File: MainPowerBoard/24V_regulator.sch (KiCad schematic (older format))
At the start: 14 parts, among them U1 LMR16030S

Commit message: Updated 5V regulator. Added 0Ohm resistors for all signals. Added protection zeners and diodes on battery inputs and on regulator outputs. TODO: Finish component selection.
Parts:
- removed R1: 45.3k, Resistors_SMD:R_1206_HandSoldering, symbol R
- added D203: 18V, symbol ZENER
- added D204: 30V, symbol ZENER
- added D205: DIODE, symbol DIODE
- added R201: 0, symbol R
- added R202: 47.5k, Resistors_SMD:R_1206_HandSoldering, symbol R
- L201: renamed from L1; value INDUCTOR -> 39uH
- renumbered C1 to C201, C2 to C202, C3 to C203, C4 to C204, C5 to C205, C6 to C206, D1 to D201, D2 to D202, R2 to R203, R2 to R204, U1 to U201, VR1 to VR201
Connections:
- wire segments 36 -> 44
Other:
- note removed: "Make these 1206 SMT"
- moved on the sheet: R1404

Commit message: Updated MainPowerBoard with various component footings. Added protective circuitry. Revised minor design elements.
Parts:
- removed D202: LED, hyperCustom:D_1206_HandSoldering, symbol LED-RESCUE-MainPowerBoard
- added D?: GREEN, LEDs:LED_1206, symbol LED

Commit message: Added all standard footprints to components. Finalized protection circuitry and indicator circuits.
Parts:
- removed D205: DIODE, symbol DIODE
- D203: footprint (none) -> Diodes_SMD:SMB_Handsoldering; DigiKey PN (none) -> 1SMB5931B-13DICT-ND; Mfg. (none) -> Diodes; Mfg. PN (none) -> 1SMB5931B-13
- D204: footprint (none) -> Diodes_SMD:SMB_Handsoldering; DigiKey PN (none) -> 3SMBJ5936BTPMSCT-ND; Mfg. (none) -> Micro; Mfg. PN (none) -> 3SMBJ5936B-TP
- R201: DigiKey PN (none) -> 311-0.0ERCT-ND; Mfg. (none) -> Yageo; Mfg. PN (none) -> RC1206JR-070RL
- U201: DigiKey PN (none) -> 296-44514-5-ND; Mfg. (none) -> Texas Instruments; Mfg. PN (none) -> LMR16030SDDA
- gave numbers to parts that had none: 1
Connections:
- wire segments 44 -> 42

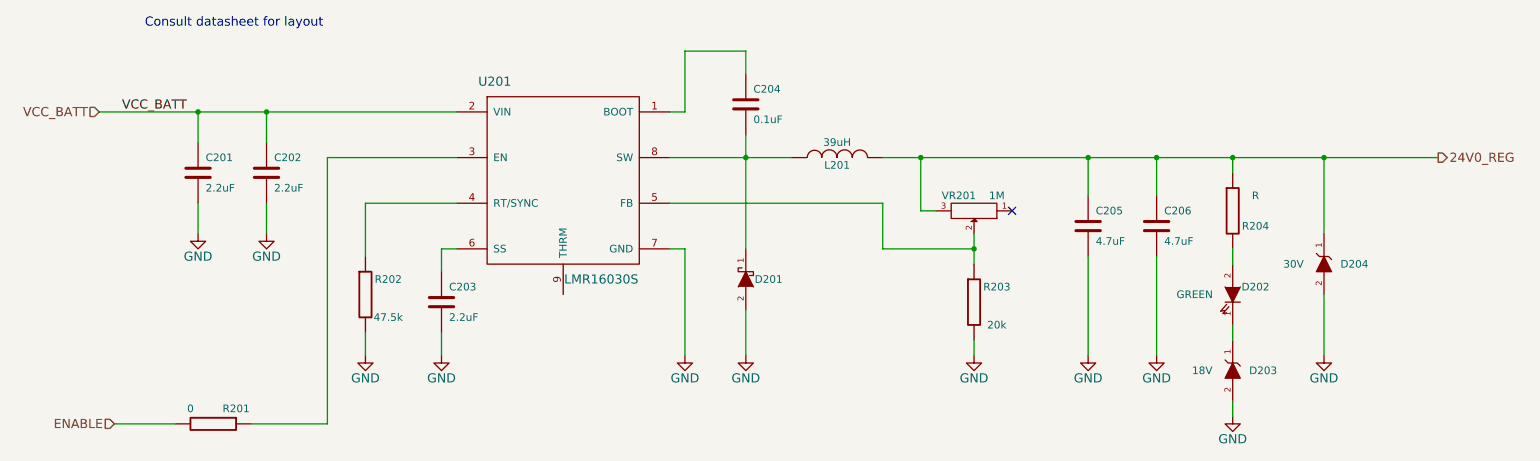
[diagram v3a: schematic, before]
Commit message: Minor changes to MainPowerBoard. About to start layout.
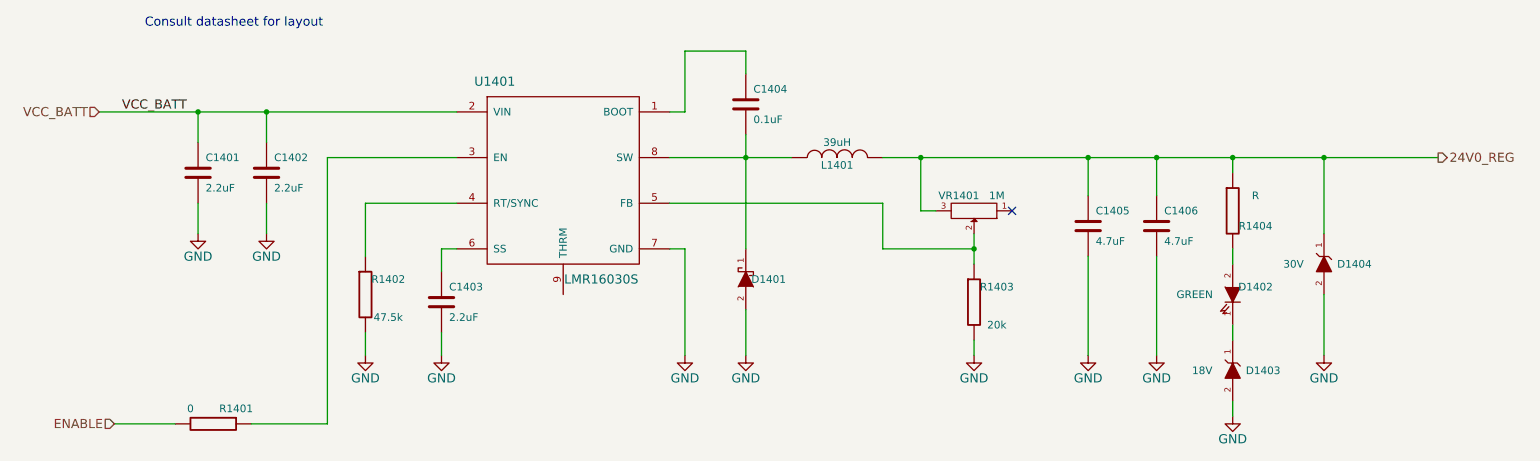
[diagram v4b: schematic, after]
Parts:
- U201: footprint (none) -> LMR16030S_8-PowerSOIC_TI.kicad_mod
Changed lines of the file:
@@
 AR Path="/583A9416/5833A728" Ref="R1304"  Part="1"
 AR Path="/583A941B/5833A728" Ref="R1404"  Part="1"
-F 0 "R204" H 8750 3950 50  0000 C CNN
+F 0 "R1404" H 8750 3950 50  0000 C CNN
 F 1 "R" H 8750 4150 50  0000 C CNN
 F 2 "Resistors_SMD:R_1210" V 8530 4050 30  0001 C CNN
@@
 AR Path="/583A9416/583A8678" Ref="U1301"  Part="1"
 AR Path="/583A941B/583A8678" Ref="U1401"  Part="1"
-F 0 "U201" H 3750 4500 60  0000 C CNN
+F 0 "U1401" H 3750 4500 60  0000 C CNN
 F 1 "LMR16030S" H 4450 3200 60  0000 C CNN
-F 2 "" H 4150 3850 60  0000 C CNN
+F 2 "LMR16030S_8-PowerSOIC_TI.kicad_mod" H 4150 3850 60  0001 C CNN
 F 3 "" H 4150 3850 60  0000 C CNN
 F 4 "Texas Instruments" H 4150 3850 60  0001 C CNN "Mfg."
@@
 AR Path="/583A9416/583A8A9A" Ref="C1301"  Part="1"
 AR Path="/583A941B/583A8A9A" Ref="C1401"  Part="1"
-F 0 "C201" H 1850 3900 50  0000 L CNN
+F 0 "C1401" H 1850 3900 50  0000 L CNN
 F 1 "2.2uF" H 1850 3700 50  0000 L CNN
 F 2 "Capacitors_SMD:C_1210_HandSoldering" H 1838 3650 30  0001 C CNN
@@
 AR Path="/583A9416/583A8B4B" Ref="C1302"  Part="1"
 AR Path="/583A941B/583A8B4B" Ref="C1402"  Part="1"
-F 0 "C202" H 2300 3900 50  0000 L CNN
+F 0 "C1402" H 2300 3900 50  0000 L CNN
 F 1 "2.2uF" H 2300 3700 50  0000 L CNN
 F 2 "Capacitors_SMD:C_1210_HandSoldering" H 2288 3650 30  0001 C CNN
@@
 AR Path="/583A9416/583A8BF8" Ref="#PWR1301"  Part="1"
 AR Path="/583A941B/583A8BF8" Ref="#PWR1401"  Part="1"
-F 0 "#PWR201" H 1800 3950 60  0001 C CNN
+F 0 "#PWR1401" H 1800 3950 60  0001 C CNN
 F 1 "GND" H 1800 4050 60  0000 C CNN
 F 2 "" H 1800 4200 60  0000 C CNN
@@
 AR Path="/583A9416/583A8C28" Ref="#PWR1302"  Part="1"
 AR Path="/583A941B/583A8C28" Ref="#PWR1402"  Part="1"
-F 0 "#PWR202" H 2250 3950 60  0001 C CNN
+F 0 "#PWR1402" H 2250 3950 60  0001 C CNN
 F 1 "GND" H 2250 4050 60  0000 C CNN
 F 2 "" H 2250 4200 60  0000 C CNN
@@
 AR Path="/583A9416/583A8CF1" Ref="C1303"  Part="1"
 AR Path="/583A941B/583A8CF1" Ref="C1403"  Part="1"
-F 0 "C203" H 3450 4750 50  0000 L CNN
+F 0 "C1403" H 3450 4750 50  0000 L CNN
 F 1 "2.2uF" H 3450 4550 50  0000 L CNN
 F 2 "Resistors_SMD:R_0805_HandSoldering" H 3438 4500 30  0001 C CNN
@@
 AR Path="/583A9416/583A8E72" Ref="#PWR1303"  Part="1"
 AR Path="/583A941B/583A8E72" Ref="#PWR1403"  Part="1"
-F 0 "#PWR203" H 2900 4750 60  0001 C CNN
+F 0 "#PWR1403" H 2900 4750 60  0001 C CNN
 F 1 "GND" H 2900 4850 60  0000 C CNN
 F 2 "" H 2900 5000 60  0000 C CNN
@@
 AR Path="/583A9416/583A8EBE" Ref="#PWR1304"  Part="1"
 AR Path="/583A941B/583A8EBE" Ref="#PWR1404"  Part="1"
-F 0 "#PWR204" H 3400 4750 60  0001 C CNN
+F 0 "#PWR1404" H 3400 4750 60  0001 C CNN
 F 1 "GND" H 3400 4850 60  0000 C CNN
 F 2 "" H 3400 5000 60  0000 C CNN
@@
 AR Path="/583A9416/583B27BB" Ref="#PWR1305"  Part="1"
 AR Path="/583A941B/583B27BB" Ref="#PWR1405"  Part="1"
-F 0 "#PWR205" H 5000 4750 60  0001 C CNN
+F 0 "#PWR1405" H 5000 4750 60  0001 C CNN
 F 1 "GND" H 5000 4850 60  0000 C CNN
 F 2 "" H 5000 5000 60  0000 C CNN
@@
 AR Path="/583A9416/583B2967" Ref="R1303"  Part="1"
 AR Path="/583A941B/583B2967" Ref="R1403"  Part="1"
-F 0 "R203" H 7050 4750 50  0000 C CNN
+F 0 "R1403" H 7050 4750 50  0000 C CNN
 F 1 "20k" H 7050 4500 50  0000 C CNN
 F 2 "Resistors_SMD:R_1206_HandSoldering" V 6830 4650 30  0001 C CNN
@@
 AR Path="/583A9416/583B2A2E" Ref="VR1301"  Part="1"
 AR Path="/583A941B/583B2A2E" Ref="VR1401"  Part="1"
-F 0 "VR201" H 7000 3950 50  0000 C CNN
+F 0 "VR1401" H 7000 3950 50  0000 C CNN
 F 1 "1M" H 6750 3950 50  0000 C CNN
 F 2 "" H 6900 4050 60  0000 C CNN
@@
 AR Path="/583A9416/583B2BCB" Ref="D1301"  Part="1"
 AR Path="/583A941B/583B2BCB" Ref="D1401"  Part="1"
-F 0 "D201" V 5400 4350 50  0000 C CNN
+F 0 "D1401" V 5400 4350 50  0000 C CNN
 F 1 "DIODESCH" H 5400 4400 50  0001 C CNN
 F 2 "Diodes_SMD:SMA_Handsoldering" H 5400 4500 60  0001 C CNN
@@
 AR Path="/583A9416/583B2C66" Ref="#PWR1306"  Part="1"
 AR Path="/583A941B/583B2C66" Ref="#PWR1406"  Part="1"
-F 0 "#PWR206" H 5400 4750 60  0001 C CNN
+F 0 "#PWR1406" H 5400 4750 60  0001 C CNN
 F 1 "GND" H 5400 4850 60  0000 C CNN
 F 2 "" H 5400 5000 60  0000 C CNN
@@
 AR Path="/583A9416/583B2D59" Ref="L1301"  Part="1"
 AR Path="/583A941B/583B2D59" Ref="L1401"  Part="1"
-F 0 "L201" V 5950 3700 50  0000 C CNN
+F 0 "L1401" V 5950 3700 50  0000 C CNN
 F 1 "39uH" V 6100 3700 50  0000 C CNN
 F 2 "" H 6000 3700 60  0000 C CNN
@@
 AR Path="/583A9416/583B307C" Ref="#PWR1307"  Part="1"
 AR Path="/583A941B/583B307C" Ref="#PWR1407"  Part="1"
-F 0 "#PWR207" H 6900 4750 60  0001 C CNN
+F 0 "#PWR1407" H 6900 4750 60  0001 C CNN
 F 1 "GND" H 6900 4850 60  0000 C CNN
 F 2 "" H 6900 5000 60  0000 C CNN
@@
 AR Path="/583A9416/583B399E" Ref="C1304"  Part="1"
 AR Path="/583A941B/583B399E" Ref="C1404"  Part="1"
-F 0 "C204" H 5450 3450 50  0000 L CNN
+F 0 "C1404" H 5450 3450 50  0000 L CNN
 F 1 "0.1uF" H 5450 3250 50  0000 L CNN
 F 2 "Resistors_SMD:R_1206_HandSoldering" H 5438 3200 30  0001 C CNN
@@
 AR Path="/583A9416/583B4188" Ref="C1305"  Part="1"
 AR Path="/583A941B/583B4188" Ref="C1405"  Part="1"
-F 0 "C205" H 7700 4250 50  0000 L CNN
+F 0 "C1405" H 7700 4250 50  0000 L CNN
 F 1 "4.7uF" H 7700 4050 50  0000 L CNN
 F 2 "Capacitors_SMD:C_1206_HandSoldering" H 7688 4000 30  0001 C CNN
@@
 AR Path="/583A9416/583B42A9" Ref="#PWR1308"  Part="1"
 AR Path="/583A941B/583B42A9" Ref="#PWR1408"  Part="1"
-F 0 "#PWR208" H 7650 4750 60  0001 C CNN
+F 0 "#PWR1408" H 7650 4750 60  0001 C CNN
 F 1 "GND" H 7650 4850 60  0000 C CNN
 F 2 "" H 7650 5000 60  0000 C CNN
@@
 AR Path="/583A9416/583B43AD" Ref="C1306"  Part="1"
 AR Path="/583A941B/583B43AD" Ref="C1406"  Part="1"
-F 0 "C206" H 8150 4250 50  0000 L CNN
+F 0 "C1406" H 8150 4250 50  0000 L CNN
 F 1 "4.7uF" H 8150 4050 50  0000 L CNN
 F 2 "Capacitors_SMD:C_1206_HandSoldering" H 8138 4000 30  0001 C CNN
@@
 AR Path="/583A9416/583B449E" Ref="#PWR1309"  Part="1"
 AR Path="/583A941B/583B449E" Ref="#PWR1409"  Part="1"
-F 0 "#PWR209" H 8100 4750 60  0001 C CNN
+F 0 "#PWR1409" H 8100 4750 60  0001 C CNN
 F 1 "GND" H 8100 4850 60  0000 C CNN
 F 2 "" H 8100 5000 60  0000 C CNN
@@
 AR Path="/583A9416/583D36BC" Ref="R1301"  Part="1"
 AR Path="/583A941B/583D36BC" Ref="R1401"  Part="1"
-F 0 "R201" V 1800 5600 50  0000 C CNN
+F 0 "R1401" V 1800 5600 50  0000 C CNN
 F 1 "0" V 1800 5300 50  0000 C CNN
 F 2 "" V 1830 5450 30  0000 C CNN
@@
 AR Path="/583A9416/583D8D48" Ref="D1303"  Part="1"
 AR Path="/583A941B/583D8D48" Ref="D1403"  Part="1"
-F 0 "D203" V 8600 4900 50  0000 C CNN
+F 0 "D1403" V 8600 4900 50  0000 C CNN
 F 1 "18V" V 8600 5300 50  0000 C CNN
 F 2 "Diodes_SMD:SMB_Handsoldering" H 8600 5100 60  0001 C CNN
@@
 AR Path="/583A9416/583D8F40" Ref="#PWR1310"  Part="1"
 AR Path="/583A941B/583D8F40" Ref="#PWR1410"  Part="1"
-F 0 "#PWR210" H 8600 5150 60  0001 C CNN
+F 0 "#PWR1410" H 8600 5150 60  0001 C CNN
 F 1 "GND" H 8600 5250 60  0000 C CNN
 F 2 "" H 8600 5400 60  0000 C CNN
@@
 AR Path="/583A9416/583D986C" Ref="D1304"  Part="1"
 AR Path="/583A941B/583D986C" Ref="D1404"  Part="1"
-F 0 "D204" V 9200 4200 50  0000 C CNN
+F 0 "D1404" V 9200 4200 50  0000 C CNN
 F 1 "30V" V 9200 4600 50  0000 C CNN
 F 2 "Diodes_SMD:SMB_Handsoldering" H 9200 4400 60  0001 C CNN
@@
 AR Path="/583A9416/583D98F6" Ref="#PWR1311"  Part="1"
 AR Path="/583A941B/583D98F6" Ref="#PWR1411"  Part="1"
-F 0 "#PWR211" H 9200 4750 60  0001 C CNN
+F 0 "#PWR1411" H 9200 4750 60  0001 C CNN
 F 1 "GND" H 9200 4850 60  0000 C CNN
 F 2 "" H 9200 5000 60  0000 C CNN
@@
 AR Path="/583A9416/583E258D" Ref="R1302"  Part="1"
 AR Path="/583A941B/583E258D" Ref="R1402"  Part="1"
-F 0 "R202" H 3050 4700 50  0000 C CNN
+F 0 "R1402" H 3050 4700 50  0000 C CNN
 F 1 "47.5k" H 3050 4450 50  0000 C CNN
 F 2 "Resistors_SMD:R_1206_HandSoldering" V 2830 4600 30  0001 C CNN
@@
 P 8600 4600
 AR Path="/582171B3/583D0112" Ref="D202"  Part="1"
-AR Path="/583A941B/583D0112" Ref="D?"  Part="1"
-AR Path="/583A870A/583D0112" Ref="D?"  Part="1"
-AR Path="/583A88E6/583D0112" Ref="D?"  Part="1"
-AR Path="/583A8D1D/583D0112" Ref="D?"  Part="1"
-F 0 "D202" V 8550 4750 50  0000 C CNN
+AR Path="/583A870A/583D0112" Ref="D802"  Part="1"
+AR Path="/583A88E6/583D0112" Ref="D902"  Part="1"
+AR Path="/583A8D1D/583D0112" Ref="D1002"  Part="1"
+AR Path="/583A8D22/583D0112" Ref="D1102"  Part="1"
+AR Path="/583A8D27/583D0112" Ref="D1202"  Part="1"
+AR Path="/583A9416/583D0112" Ref="D1302"  Part="1"
+AR Path="/583A941B/583D0112" Ref="D1402"  Part="1"
+F 0 "D1402" V 8550 4750 50  0000 C CNN
 F 1 "GREEN" V 8600 4350 50  0000 C CNN
 F 2 "LEDs:LED_1206" H 8600 4600 60  0001 C CNN

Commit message: Began MainPowerBoard layout. Decided on final size of 7x7. Placed battery connectors. Finalized almost all footprints. Laid out one regulator circuit. TODO: Finish regulator layout; duplicate it; pick higher current connector for AC-DC adapter.
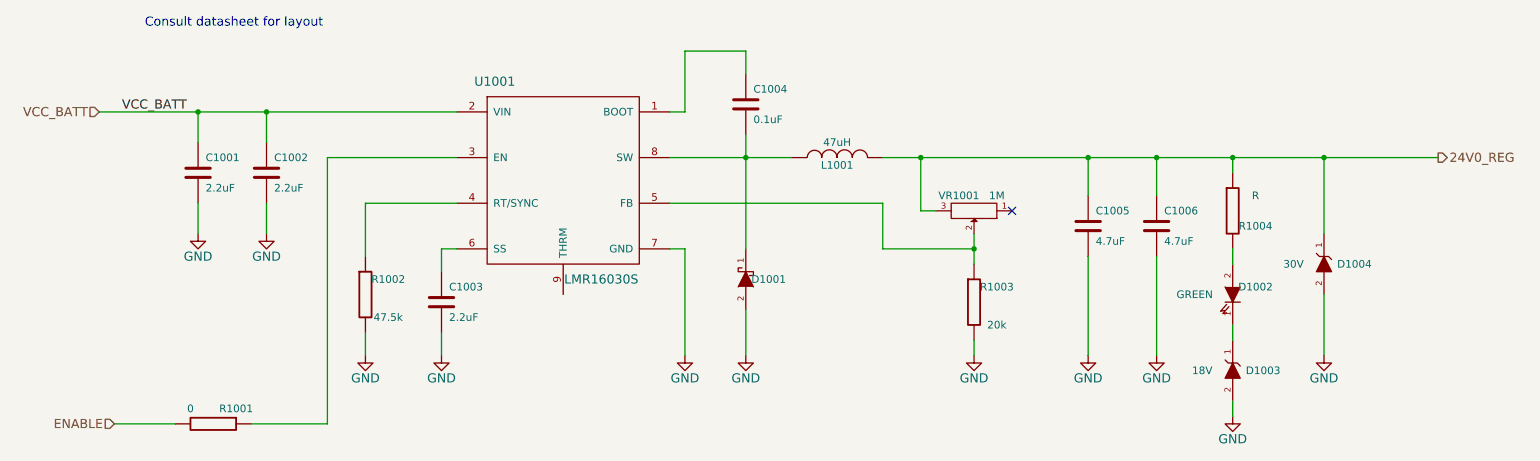
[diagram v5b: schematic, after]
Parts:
- L201: value 39uH -> 47uH; footprint (none) -> hyperCustom:47uIND_CDRH127_LDNP-470MC_SUMIDA
- R201: footprint (none) -> Resistors_SMD:R_1206_HandSoldering
- R204: footprint Resistors_SMD:R_1210 -> Resistors_SMD:R_1206_HandSoldering
- U201: footprint LMR16030S_8-PowerSOIC_TI.kicad_mod -> hyperCustom:LMR16030S_8-PowerSOIC_TI
- VR201: footprint (none) -> hyperCustom:BOURNS_MULTITURNPOT_3299W
